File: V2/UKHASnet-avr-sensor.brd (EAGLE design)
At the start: 49.5 x 49.2 mm, 34 parts, among them J1 AVR_SPI_PRG_62X3_LOCK, U1 MCP1700-3302E/TO, U2 ATMEGA328P-PU, X1 SMA-142-0711-881/886, Y1 RESONATORPTH

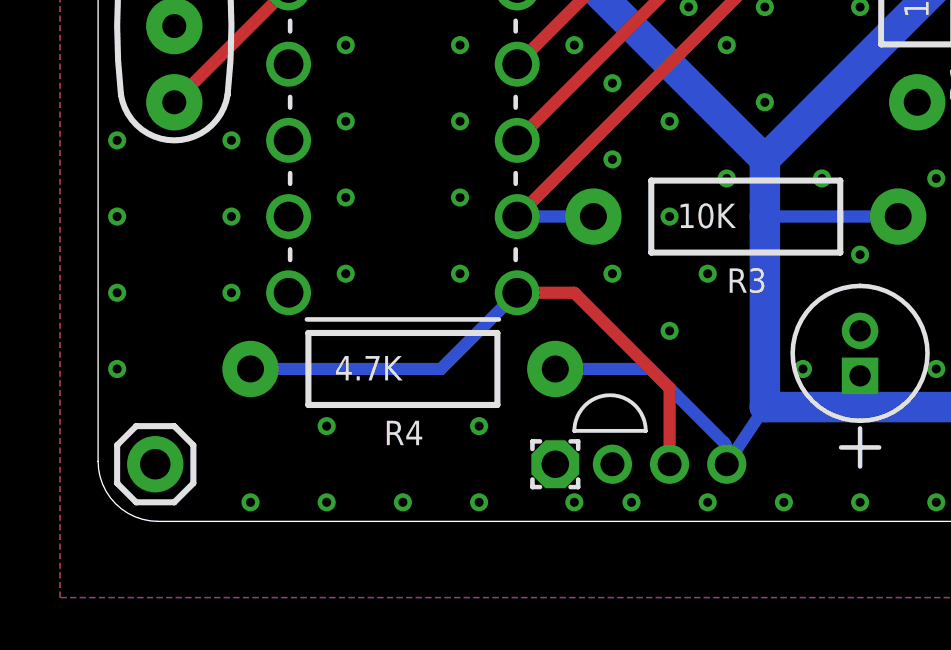
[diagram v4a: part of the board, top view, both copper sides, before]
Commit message: Drive sensor vcc from AVR PB0.
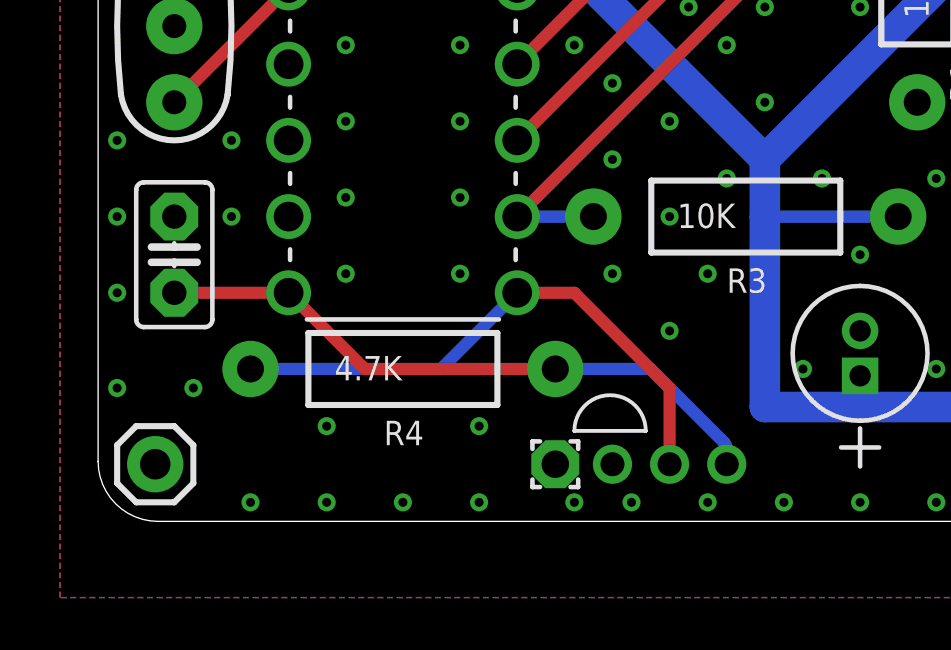
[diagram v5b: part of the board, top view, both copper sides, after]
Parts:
- added C7: 0.1uF, capacitor-wima:C2.5-2
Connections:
- new net SENSE_VCC: C7.1, R4.P$2, U$2.VDD, U2.14
- net GND: now also C7.2
- net VCC: no longer R4.P$2, U$2.VDD
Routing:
- net SENSE_VCC: track 0.00 -> 21.1 mm
- net VCC: track 122.3 -> 112.6 mm
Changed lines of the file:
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@@
 <element name="U$3" library="SparkFun-Aesthetics" package="OSHW-LOGO-M" value="" x="45.72" y="8.89" rot="R90"/>
 <element name="PAD1" library="wirepad" package="1,6/0,9" value="WIREPAD1,6/0,9" x="15.24" y="1.905" smashed="yes"/>
+<element name="C7" library="capacitor-wima" package="C2.5-2" value="0.1uF" x="2.54" y="8.89" smashed="yes" rot="R90">
+<attribute name="VALUE" x="0.889" y="5.461" size="0.8128" layer="27" font="vector" ratio="15"/>
+</element>
 </elements>
 <signals>
@@
 <contactref element="J1" pad="2"/>
 <contactref element="U1" pad="3"/>
-<contactref element="U$2" pad="VDD"/>
-<contactref element="R4" pad="P$2"/>
 <contactref element="C6" pad="1"/>
 <contactref element="C1" pad="1"/>
-<wire x1="22.225" y1="3.81" x2="20.955" y2="1.905" width="0.4064" layer="16"/>
 <contactref element="U$1" pad="VCC"/>
 <contactref element="C5" pad="1"/>
@@
 <via x="38.735" y="28.575" extent="1-16" drill="0.6"/>
 <wire x1="47.625" y1="40.8625" x2="47.625" y2="43.18" width="0.8128" layer="1"/>
-<wire x1="20.955" y1="1.905" x2="20.955" y2="2.4084875" width="0.4064" layer="16"/>
-<wire x1="20.955" y1="2.4084875" x2="20.86200625" y2="2.63299375" width="0.4064" layer="16" curve="45"/>
-<wire x1="20.86200625" y1="2.63299375" x2="18.415" y2="5.08" width="0.4064" layer="16"/>
-<wire x1="18.415" y1="5.08" x2="15.24" y2="5.08" width="0.4064" layer="16"/>
 <contactref element="JP15" pad="1"/>
 <wire x1="6.35" y1="25.4" x2="5.715" y2="25.4" width="0.8128" layer="16"/>
@@
 <via x="8.255" y="8.255" extent="1-16" drill="0.3"/>
 <via x="0.635" y="7.62" extent="1-16" drill="0.3"/>
-<via x="0.635" y="5.08" extent="1-16" drill="0.3"/>
+<via x="0.635" y="4.445" extent="1-16" drill="0.3"/>
 <via x="5.08" y="0.635" extent="1-16" drill="0.3"/>
 <via x="7.62" y="0.635" extent="1-16" drill="0.3"/>
@@
 <via x="45.085" y="38.1" extent="1-16" drill="0.3"/>
 <via x="4.445" y="10.16" extent="1-16" drill="0.3"/>
-<via x="4.445" y="7.62" extent="1-16" drill="0.3"/>
+<via x="3.175" y="4.445" extent="1-16" drill="0.3"/>
 <via x="7.62" y="3.175" extent="1-16" drill="0.3"/>
 <via x="12.7" y="3.175" extent="1-16" drill="0.3"/>
@@
 <via x="43.18" y="43.18" extent="1-16" drill="0.3"/>
 <contactref element="PAD1" pad="1"/>
+<contactref element="C7" pad="2"/>
 </signal>
 <signal name="VIN">
@@
 <wire x1="13.97" y1="35.56" x2="17.78" y2="39.37" width="0.4064" layer="1"/>
 </signal>
+<signal name="SENSE_VCC">
+<contactref element="U2" pad="14"/>
+<contactref element="U$2" pad="VDD"/>
+<contactref element="R4" pad="P$2"/>
+<wire x1="20.955" y1="1.905" x2="20.955" y2="2.4084875" width="0.4064" layer="16"/>
+<wire x1="20.955" y1="2.4084875" x2="20.86200625" y2="2.63299375" width="0.4064" layer="16" curve="45"/>
+<wire x1="20.86200625" y1="2.63299375" x2="18.415" y2="5.08" width="0.4064" layer="16"/>
+<wire x1="18.415" y1="5.08" x2="15.24" y2="5.08" width="0.4064" layer="16"/>
+<contactref element="C7" pad="1"/>
+<wire x1="6.35" y1="7.62" x2="2.54" y2="7.62" width="0.4064" layer="1"/>
+<wire x1="15.24" y1="5.08" x2="8.89" y2="5.08" width="0.4064" layer="1"/>
+<wire x1="8.89" y1="5.08" x2="6.35" y2="7.62" width="0.4064" layer="1"/>
+</signal>
 </signals>
